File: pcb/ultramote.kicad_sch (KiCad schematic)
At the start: 4 parts, among them J1 U.FL-R-SMT-1, U1 LoRa-E5

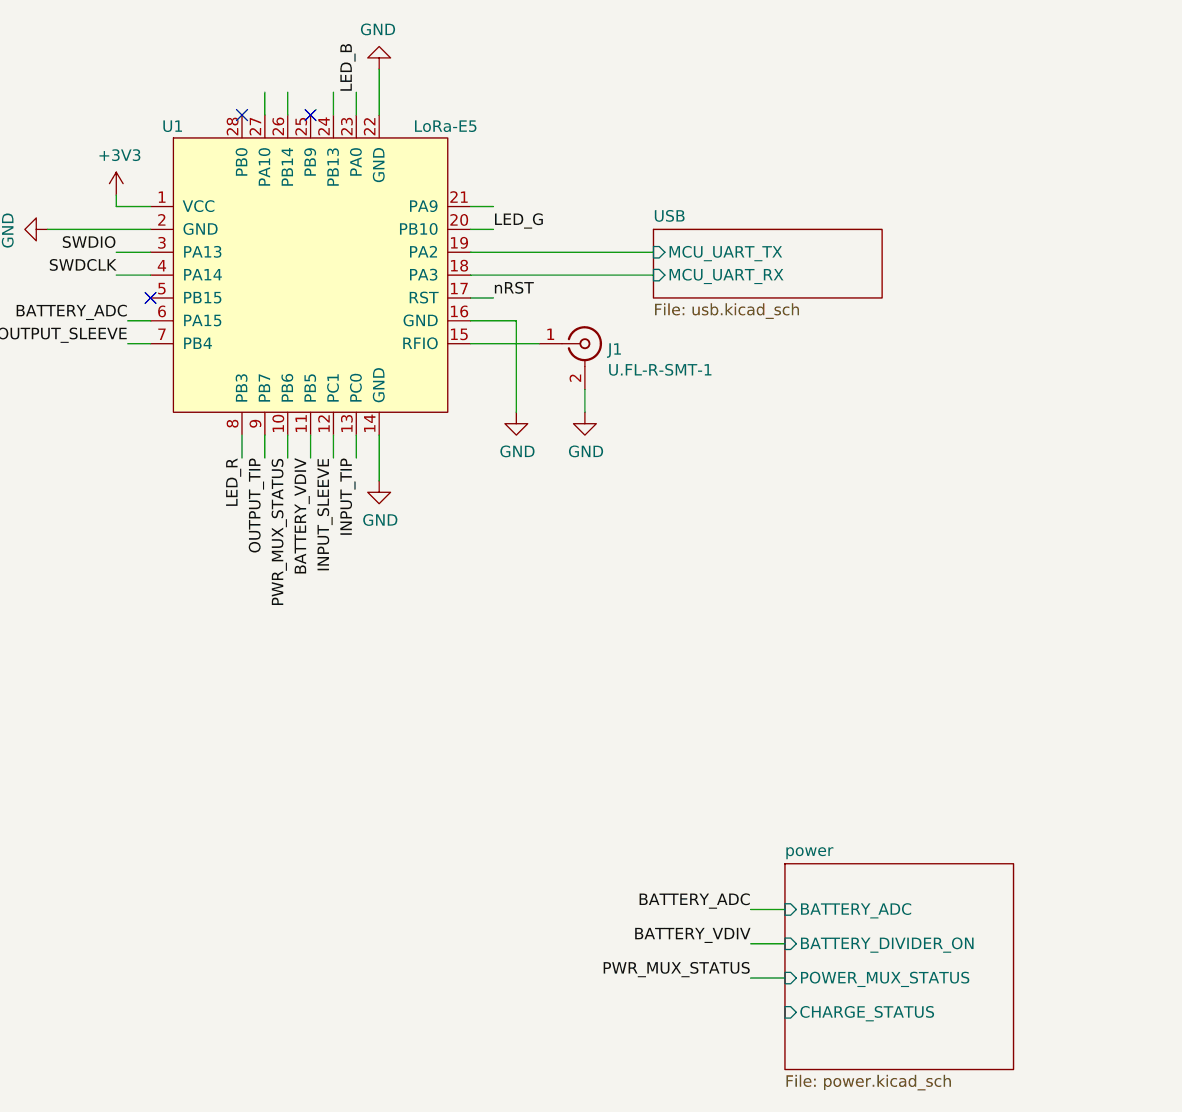
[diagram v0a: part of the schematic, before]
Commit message: Fix ERC warnings
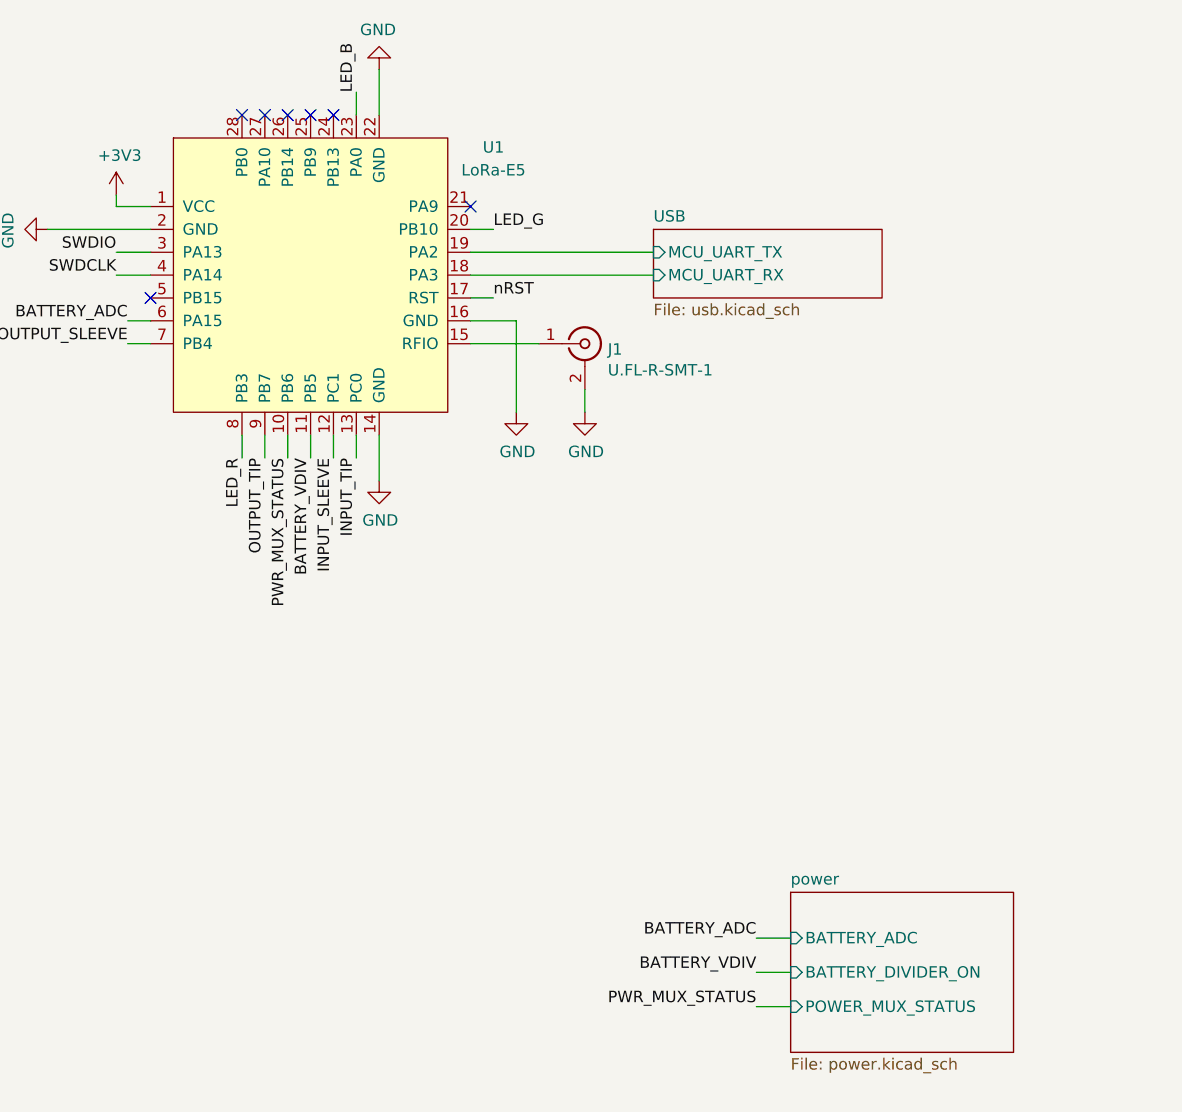
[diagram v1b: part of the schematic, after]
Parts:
- removed U1: LoRa-E5, ultramote:LoRa-E5, symbol LoRa-E5:LoRa-E5
- added U1: LoRa-E5, ultramote:LoRa-E5, symbol ultramote:LoRa-E5
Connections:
- net +3V3: now also U1.1 (VCC)
- net BATTERY_ADC: now also U1.6 (PA15)
- net BATTERY_VDIV: now also U1.11 (PB5)
- net GND: now also U1.14 (GND), U1.16 (GND), U1.2 (GND), U1.22 (GND)
- net INPUT_SLEEVE: now also U1.12 (PC1)
- net INPUT_TIP: now also U1.13 (PC0)
- net LED_B: now also U1.23 (PA0)
- net LED_G: now also U1.20 (PB10)
- net LED_R: now also U1.8 (PB3)
- net OUTPUT_SLEEVE: now also U1.7 (PB4)
- net OUTPUT_TIP: now also U1.9 (PB7)
- net PWR_MUX_STATUS: now also U1.10 (PB6)
- net SWDCLK: now also U1.4 (PA14)
- net SWDIO: now also U1.3 (PA13)
- net USB/MCU_UART_RX: now also U1.18 (PA3)
- net USB/MCU_UART_TX: now also U1.19 (PA2)
- net nRST: now also U1.17 (RST)
- net at J1.1 (In): now also U1.15 (RFIO)
- no-connect marks 3 -> 7
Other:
- sheet power ports: added none; removed CHARGE_STATUS

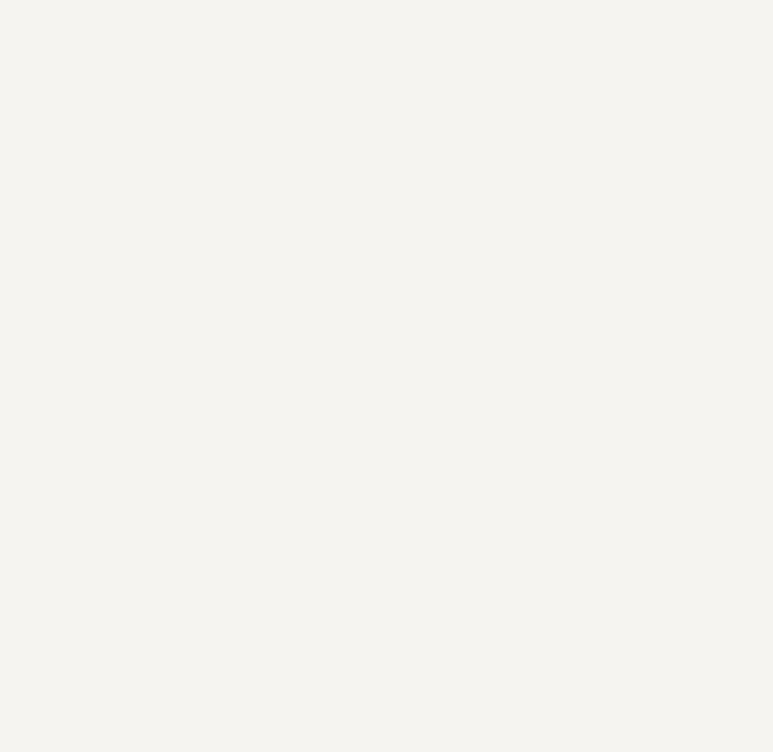
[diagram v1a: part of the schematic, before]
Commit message: Add datasheet links
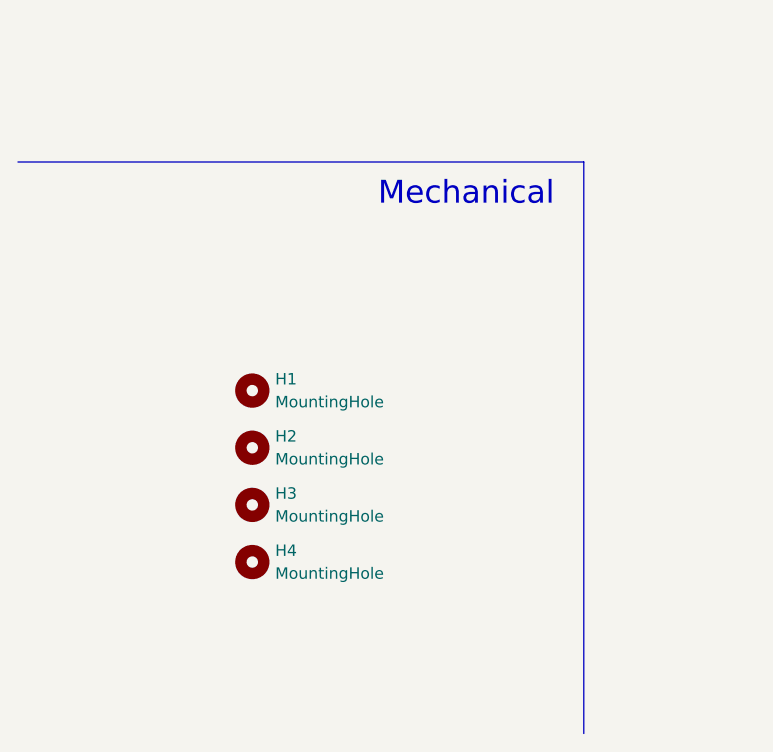
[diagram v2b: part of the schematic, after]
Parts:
- added H1, H2, H3, H4: MountingHole, MountingHole:MountingHole_2.2mm_M2, symbol Mechanical:MountingHole
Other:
- note added: "Mechanical"
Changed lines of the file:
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@@
+    (stroke (width 0) (type default) (color 0 0 0 0))
+  )
+  (polyline (pts (xy 12.7 133.35) (xy 75.565 133.35))
     (stroke (width 0) (type default) (color 0 0 0 0))
   )
@@
     (stroke (width 0) (type default) (color 0 0 0 0))
   )
+  (polyline (pts (xy 75.565 133.35) (xy 75.565 196.85))
+    (stroke (width 0) (type default) (color 0 0 0 0))
+  )
   (wire (pts (xy 77.47 60.325) (xy 81.28 60.325))
     (stroke (width 0) (type default) (color 0 0 0 0))
@@
   (wire (pts (xy 237.49 128.27) (xy 241.3 128.27))
     (stroke (width 0) (type default) (color 0 0 0 0))
+  )
+  (text "Mechanical" (at 52.705 138.43 0)
+    (effects (font (size 2.54 2.54)) (justify left bottom))
   )
   (label "LED_G" (at 241.3 143.51 0)
@@
       (effects (font (size 1.27 1.27)) hide)
     )
-    (property "Datasheet" " ~" (id 3) (at 129.54 67.945 0)
+    (property "Datasheet" "https://datasheet.lcsc.com/lcsc/1811091710_HRS-Hirose-U-FL-R-SMT-1-80_C88374.pdf" (id 3) (at 129.54 67.945 0)
       (effects (font (size 1.27 1.27)) hide)
     )
@@
       (effects (font (size 1.27 1.27)) hide)
     )
-    (property "Datasheet" "" (id 3) (at 99.06 60.325 0)
+    (property "Datasheet" "https://files.seeedstudio.com/products/317990687/res/LoRa-E5%20module%20datasheet_V1.0.pdf" (id 3) (at 99.06 60.325 0)
       (effects (font (size 1.27 1.27)) hide)
     )
@@
     (pin "9")
   )
+  (symbol (lib_id "Mechanical:MountingHole") (at 38.735 171.45 0) (unit 1)
+    (in_bom yes) (on_board yes) (fields_autoplaced)
+    (property "Reference" "H3" (id 0) (at 41.275 170.1799 0)
+      (effects (font (size 1.27 1.27)) (justify left))
+    )
+    (property "Value" "MountingHole" (id 1) (at 41.275 172.7199 0)
+      (effects (font (size 1.27 1.27)) (justify left))
+    )
+    (property "Footprint" "MountingHole:MountingHole_2.2mm_M2" (id 2) (at 38.735 171.45 0)
+      (effects (font (size 1.27 1.27)) hide)
+    )
+    (property "Datasheet" "~" (id 3) (at 38.735 171.45 0)
+      (effects (font (size 1.27 1.27)) hide)
+    )
+  )
+  (symbol (lib_id "Mechanical:MountingHole") (at 38.735 158.75 0) (unit 1)
+    (in_bom yes) (on_board yes) (fields_autoplaced)
+    (property "Reference" "H1" (id 0) (at 41.275 157.4799 0)
+      (effects (font (size 1.27 1.27)) (justify left))
+    )
+    (property "Value" "MountingHole" (id 1) (at 41.275 160.0199 0)
+      (effects (font (size 1.27 1.27)) (justify left))
+    )
+    (property "Footprint" "MountingHole:MountingHole_2.2mm_M2" (id 2) (at 38.735 158.75 0)
+      (effects (font (size 1.27 1.27)) hide)
+    )
+    (property "Datasheet" "~" (id 3) (at 38.735 158.75 0)
+      (effects (font (size 1.27 1.27)) hide)
+    )
+  )
+  (symbol (lib_id "Mechanical:MountingHole") (at 38.735 177.8 0) (unit 1)
+    (in_bom yes) (on_board yes) (fields_autoplaced)
+    (property "Reference" "H4" (id 0) (at 41.275 176.5299 0)
+      (effects (font (size 1.27 1.27)) (justify left))
+    )
+    (property "Value" "MountingHole" (id 1) (at 41.275 179.0699 0)
+      (effects (font (size 1.27 1.27)) (justify left))
+    )
+    (property "Footprint" "MountingHole:MountingHole_2.2mm_M2" (id 2) (at 38.735 177.8 0)
+      (effects (font (size 1.27 1.27)) hide)
+    )
+    (property "Datasheet" "~" (id 3) (at 38.735 177.8 0)
+      (effects (font (size 1.27 1.27)) hide)
+    )
+  )
+  (symbol (lib_id "Mechanical:MountingHole") (at 38.735 165.1 0) (unit 1)
+    (in_bom yes) (on_board yes) (fields_autoplaced)
+    (property "Reference" "H2" (id 0) (at 41.275 163.8299 0)
+      (effects (font (size 1.27 1.27)) (justify left))
+    )
+    (property "Value" "MountingHole" (id 1) (at 41.275 166.3699 0)
+      (effects (font (size 1.27 1.27)) (justify left))
+    )
+    (property "Footprint" "MountingHole:MountingHole_2.2mm_M2" (id 2) (at 38.735 165.1 0)
+      (effects (font (size 1.27 1.27)) hide)
+    )
+    (property "Datasheet" "~" (id 3) (at 38.735 165.1 0)
+      (effects (font (size 1.27 1.27)) hide)
+    )
+  )
   (sheet (at 137.16 55.245) (size 25.4 7.62) (fields_autoplaced)
     (stroke (width 0.1524) (type solid) (color 0 0 0 0))
@@
       (reference "FB1") (unit 1) (value "MMZ1608B601CTAH0") (footprint "Capacitor_SMD:C_0603_1608Metric")
     )
+    (path "/10905177-5580-4814-aa5a-26155f4d07e8"
+      (reference "H1") (unit 1) (value "MountingHole") (footprint "MountingHole:MountingHole_2.2mm_M2")
+    )
+    (path "/f2eee90b-8814-42b4-84cc-0f588beb639f"
+      (reference "H2") (unit 1) (value "MountingHole") (footprint "MountingHole:MountingHole_2.2mm_M2")
+    )
+    (path "/0f158ad0-c08b-4489-8148-bc426d69c023"
+      (reference "H3") (unit 1) (value "MountingHole") (footprint "MountingHole:MountingHole_2.2mm_M2")
+    )
+    (path "/304bc48f-1e6d-46a6-932a-449f3b8bcf80"
+      (reference "H4") (unit 1) (value "MountingHole") (footprint "MountingHole:MountingHole_2.2mm_M2")
+    )
     (path "/00000000-0000-0000-0000-000062077d98"
       (reference "J1") (unit 1) (value "U.FL-R-SMT-1") (footprint "Connector_Coaxial:U.FL_Hirose_U.FL-R-SMT-1_Vertical")
     )
     (path "/a94f32ff-7dd8-43e8-b716-e2ddbd1741de/0356246a-22c4-42ca-89c4-4d782319d515"
-      (reference "J2") (unit 1) (value "SM02B-SRSS-TB") (footprint "Connector_JST:JST_PH_B2B-PH-SM4-TB_1x02-1MP_P2.00mm_Vertical")
+      (reference "J2") (unit 1) (value "SM02B-SRSS-TB") (footprint "Connector_JST:JST_SH_SM02B-SRSS-TB_1x02-1MP_P1.00mm_Horizontal")
     )
     (path "/168e6a28-0e03-4606-8c7b-f849efe47418/fdd0219c-ee93-4242-b587-cabb3ac9b47b"
-      (reference "J3") (unit 1) (value "918-418K2023S40001") (footprint "ultramote:USB_C_Receptacle_XKB_U262-16XN-4BVC11")
+      (reference "J3") (unit 1) (value "USB-C-XKB_U262-16XN") (footprint "ultramote:USB_C_Receptacle_XKB_U262-16XN-4BVC11")
     )
     (path "/43fad132-fb74-49a6-968f-ee47e7e9e12e/a7139d86-afe3-4b7f-b3e9-e49c8cb860d8"
-      (reference "J5") (unit 1) (value "Conn_01x04") (footprint "ultramote:WR_WST-REDFIT-4P_DEBUG")
+      (reference "J5") (unit 1) (value "WST-REDFIT-4P") (footprint "ultramote:WR_WST-REDFIT-4P_DEBUG")
     )
     (path "/43fad132-fb74-49a6-968f-ee47e7e9e12e/b152591d-58b2-4747-b4ab-60eb703f5826"

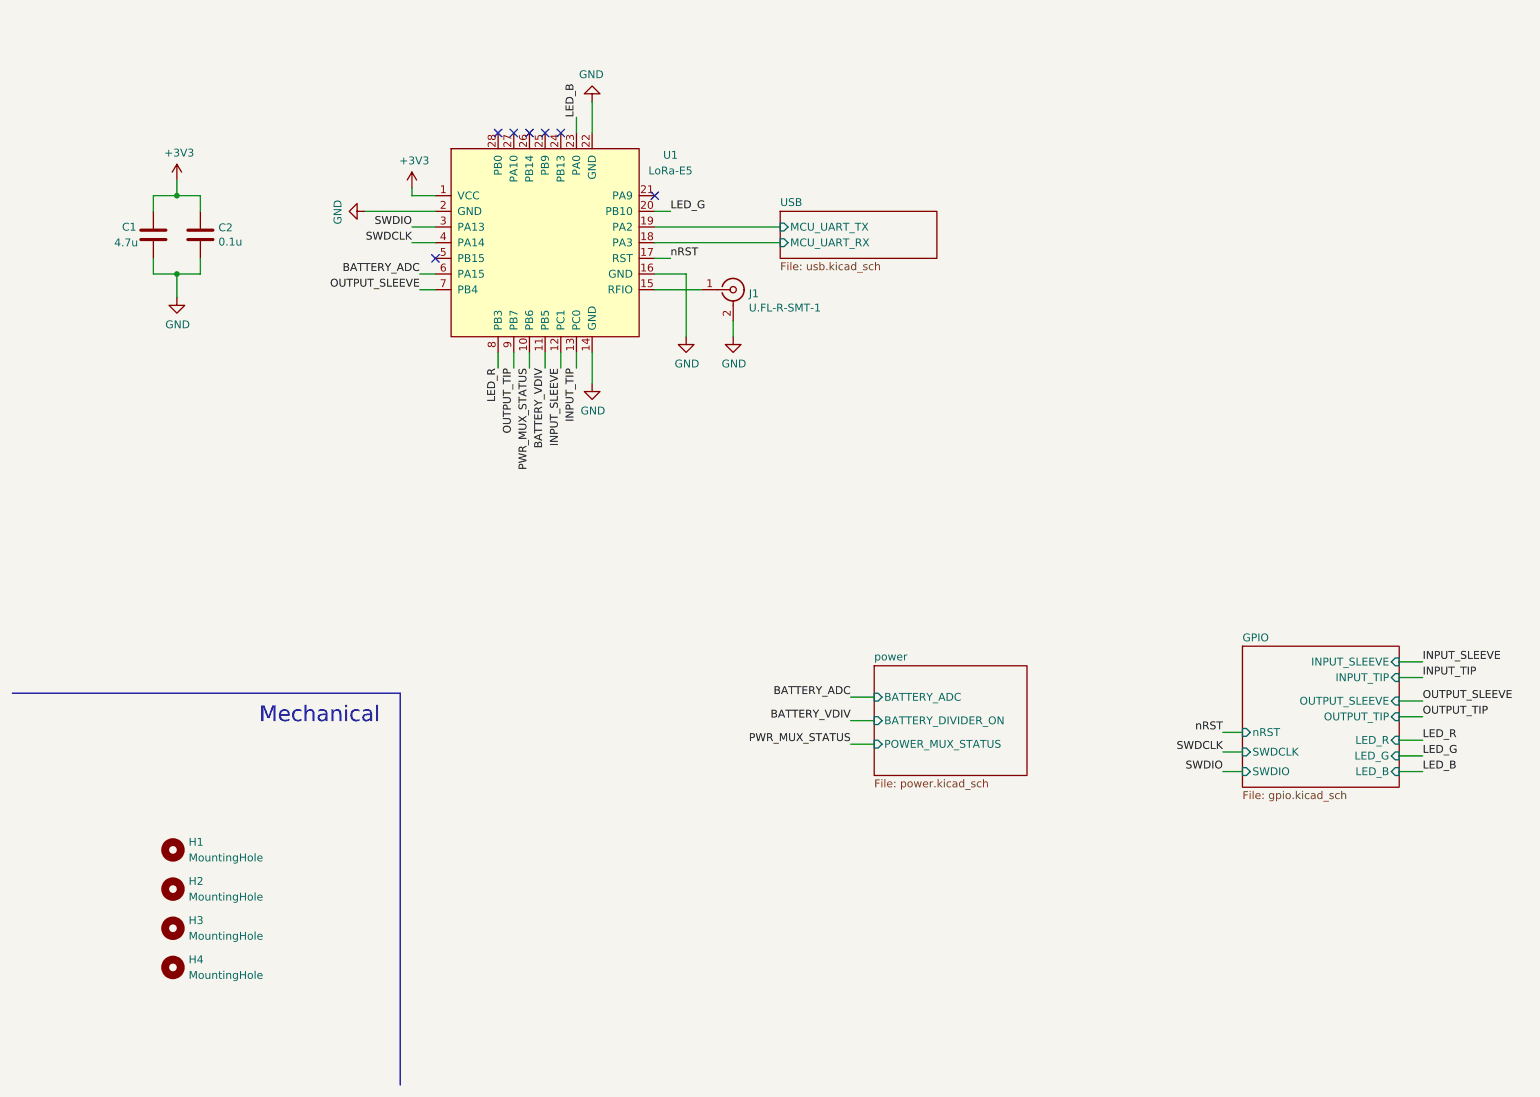
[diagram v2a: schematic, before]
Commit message: Migrate project to KiCad v7
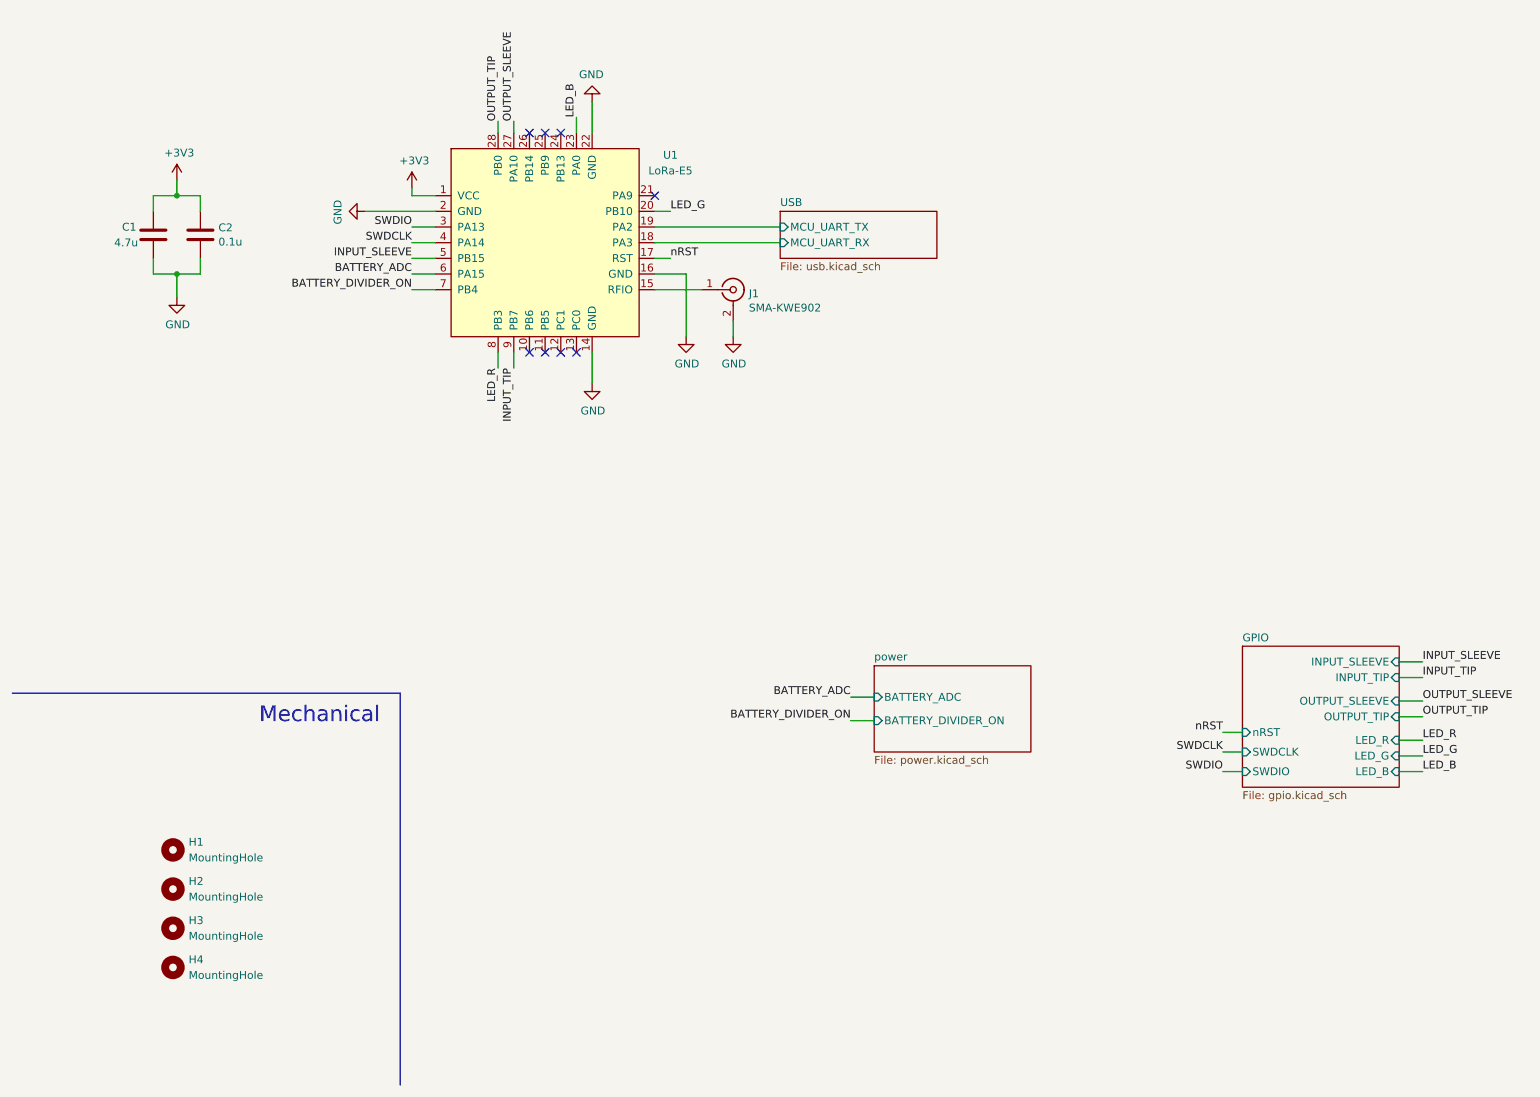
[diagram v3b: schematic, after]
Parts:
- J1: value U.FL-R-SMT-1 -> SMA-KWE902; footprint Connector_Coaxial:U.FL_Hirose_U.FL-R-SMT-1_Vertical -> ultramote:SMA-KWE902; LCSC Part Number C88374 -> C914554; Manufacturer Part Number U.FL-R-SMT-1(80) -> SMA-KE-P903
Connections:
- net INPUT_SLEEVE: now also U1.5 (PB15); no longer U1.12 (PC1)
- net INPUT_TIP: now also U1.9 (PB7); no longer U1.13 (PC0)
- net OUTPUT_SLEEVE: now also U1.27 (PA10); no longer U1.7 (PB4)
- net OUTPUT_TIP: now also U1.28 (PB0); no longer U1.9 (PB7)
- net BATTERY_VDIV: no longer names the net of U1.11 (PB5)
- net PWR_MUX_STATUS: no longer names the net of U1.10 (PB6)
- new net BATTERY_DIVIDER_ON: U1.7 (PB4)
- no-connect marks 7 -> 8
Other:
- sheet power ports: added none; removed POWER_MUX_STATUS
